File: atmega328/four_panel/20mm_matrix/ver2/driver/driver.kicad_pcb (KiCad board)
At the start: 2 copper layers, 40 x 40 mm, 52 parts, among them IC1 ATMEGA328P-M, IC2 ATMEGA328P-M, IC3 ATMEGA328P-M, IC4 ATMEGA328P-M, X1 CER_RESO, X2 CER_RESO, X3 CER_RESO, X4 CER_RESO

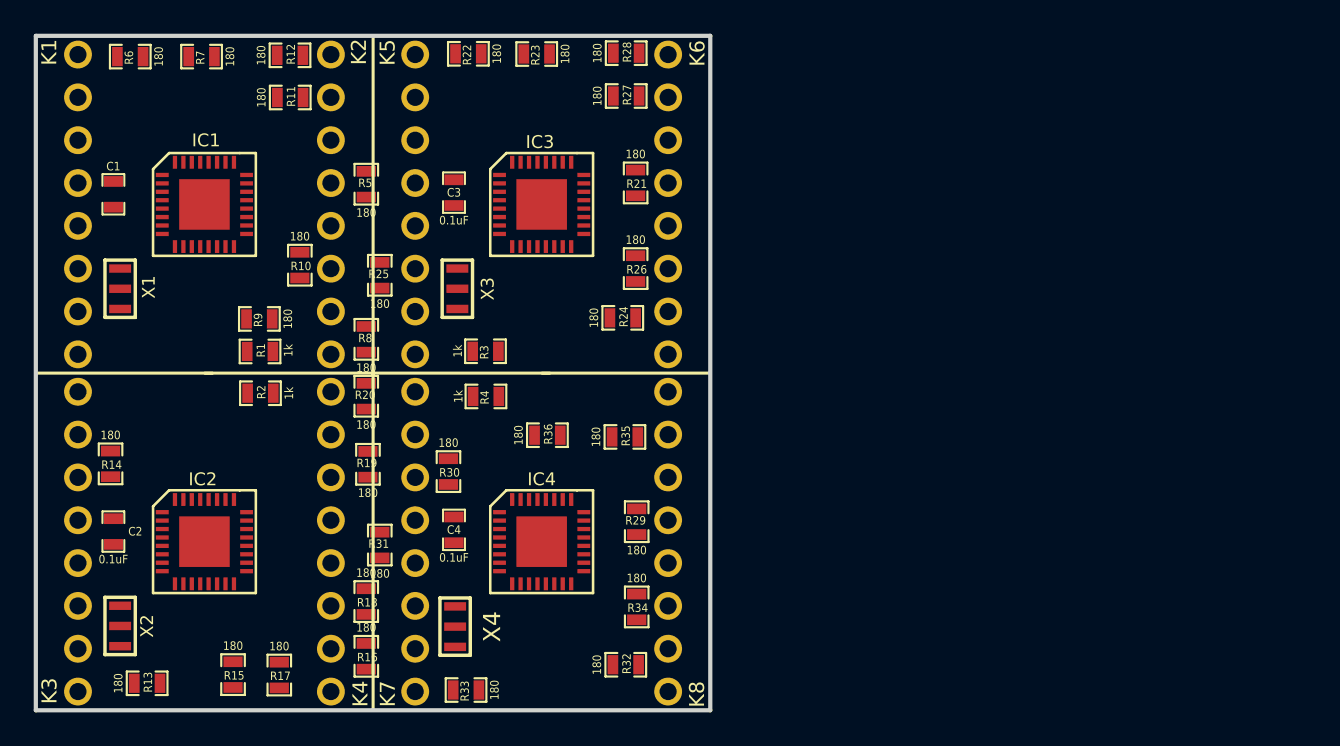
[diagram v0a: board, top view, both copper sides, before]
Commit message: Worked on ver2 of atmega328 4x20mm driver and comm pcbs.
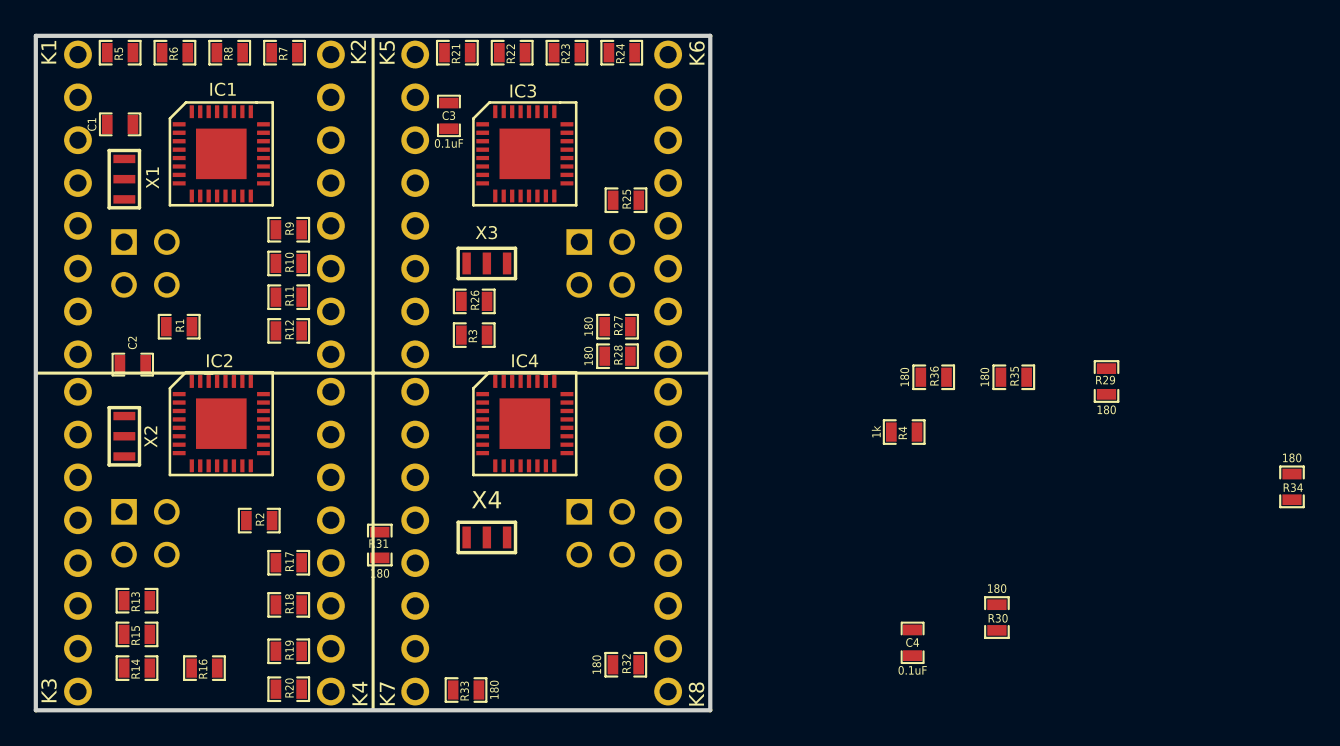
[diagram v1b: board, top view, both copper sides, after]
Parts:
- added P1: CONN_2X2, PIN_ARRAY_2X2, B.Cu at (56.5, 63.5)
- added P2: CONN_2X2, PIN_ARRAY_2X2, B.Cu at (56.5, 79.5)
- added P3: CONN_2X2, PIN_ARRAY_2X2, B.Cu at (83.5, 63.5)
- added P4: CONN_2X2, PIN_ARRAY_2X2, B.Cu at (83.5, 79.5)
- moved R34 39.5 mm to (124.5, 76.8)
- moved R30 33.7 mm to (107.0, 84.5)
- moved R29 29.1 mm to (113.5, 70.5)
- moved C4 28.0 mm to (102.0, 86.0)
- moved R4 24.9 mm to (101.5, 73.5)
- moved R35 23.3 mm to (108.0, 70.2)
- moved R36 23.2 mm to (103.2, 70.2)
- moved R8 18.8 mm to (61.5, 51.0), turned to 180 degrees
- moved R28 18.0 mm to (84.5, 69.0)
- moved R20 18.0 mm to (65.0, 88.8), turned to 0 degrees
- moved R5 16.6 mm to (55.0, 51.0), turned to 180 degrees
- moved R12 16.3 mm to (65.0, 67.5)
- moved R24 15.7 mm to (84.8, 51.0), turned to 180 degrees
- moved R25 15.3 mm to (85.0, 59.8), turned to 0 degrees
- moved R27 13.7 mm to (84.5, 67.2)
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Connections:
- net /XTAL1_DRV4 renamed /XTAL0_DRV3
- net /XTAL2_DRV1 renamed /XTAL1_DRV0
- IC1 pad 1: /COL4_DRV1 -> /ROW3_DRV0
- IC1 pad 10: /COL7_DRV1 -> /ROW6_DRV0
- IC1 pad 11: /COL8_DRV1 -> /ROW7_DRV0
- IC1 pad 12: /ROW1_DRV1 -> /COL6_DRV0
- IC1 pad 13: /ROW2_DRV1 -> /COL7_DRV0
- IC1 pad 14: /ROW3_DRV1 -> /CS0
- IC1 pad 15: /ROW4_DRV1 -> /MOSI
- IC1 pad 16: /ROW5_DRV1 -> /MISO
- IC1 pad 17: /ROW6_DRV1 -> /SCK
- IC1 pad 2: /COL5_DRV1 -> /ROW4_DRV0
- IC1 pad 23: /ROW7_DRV1 -> /COL0_DRV0
- IC1 pad 24: /ROW8_DRV1 -> /COL1_DRV0
- IC1 pad 25: /PCINT10/PC2 -> /COL2_DRV0
- IC1 pad 26: /PCINT11/PC3 -> /COL3_DRV0
- IC1 pad 27: /SDA -> /COL4_DRV0
- IC1 pad 28: /SCL -> /COL5_DRV0
- IC1 pad 29: /RESET_DRV1 -> /RESET_DRV0
- IC1 pad 30: /COL1_DRV1 -> /ROW0_DRV0
- IC1 pad 31: /COL2_DRV1 -> /ROW1_DRV0
- IC1 pad 32: /COL3_DRV1 -> /ROW2_DRV0
- IC1 pad 7: /XTAL1_DRV1 -> /XTAL0_DRV0
- IC1 pad 9: /COL6_DRV1 -> /ROW5_DRV0
- IC2 pad 1: /COL4_DRV2 -> /ROW3_DRV1
- IC2 pad 10: /COL7_DRV2 -> /ROW6_DRV1
- IC2 pad 11: /COL8_DRV2 -> /ROW7_DRV1
- IC2 pad 12: /ROW1_DRV2 -> /COL6_DRV1
- IC2 pad 13: /ROW2_DRV2 -> /COL7_DRV1
- IC2 pad 14: /ROW3_DRV2 -> /CS1
- IC2 pad 15: /ROW4_DRV2 -> /MOSI
- IC2 pad 16: /ROW5_DRV2 -> /MISO
- IC2 pad 17: /ROW6_DRV2 -> /SCK
- IC2 pad 2: /COL5_DRV2 -> /ROW4_DRV1
- IC2 pad 23: /ROW7_DRV2 -> /COL0_DRV1
- IC2 pad 24: /ROW8_DRV2 -> /COL1_DRV1
- IC2 pad 25: /PCINT10/PC2 -> /COL2_DRV1
- IC2 pad 26: /PCINT11/PC3 -> /COL3_DRV1
- IC2 pad 27: /SDA -> /COL4_DRV1
- IC2 pad 28: /SCL -> /COL5_DRV1
- IC2 pad 29: /RESET_DRV2 -> /RESET_DRV1
- IC2 pad 30: /COL1_DRV2 -> /ROW0_DRV1
- IC2 pad 31: /COL2_DRV2 -> /ROW1_DRV1
- IC2 pad 32: /COL3_DRV2 -> /ROW2_DRV1
- IC2 pad 7: /XTAL1_DRV2 -> /XTAL0_DRV1
- IC2 pad 8: /XTAL2_DRV2 -> /XTAL1_DRV1
- IC2 pad 9: /COL6_DRV2 -> /ROW5_DRV1
- IC3 pad 1: /COL4_DRV3 -> /ROW3_DRV2
- IC3 pad 10: /COL7_DRV3 -> /ROW6_DRV2
- IC3 pad 11: /COL8_DRV3 -> /ROW7_DRV2
- IC3 pad 12: /ROW1_DRV3 -> /COL6_DRV2
- IC3 pad 13: /ROW2_DRV3 -> /COL7_DRV2
- IC3 pad 14: /ROW3_DRV3 -> /CS2
- IC3 pad 15: /ROW4_DRV3 -> /MOSI
- IC3 pad 16: /ROW5_DRV3 -> /MISO
- IC3 pad 17: /ROW6_DRV3 -> /SCK
- IC3 pad 2: /COL5_DRV3 -> /ROW4_DRV2
- IC3 pad 23: /ROW7_DRV3 -> /COL0_DRV2
- IC3 pad 24: /ROW8_DRV3 -> /COL1_DRV2
- IC3 pad 25: /PCINT10/PC2 -> /COL2_DRV2
- IC3 pad 26: /PCINT11/PC3 -> /COL3_DRV2
- IC3 pad 27: /SDA -> /COL4_DRV2
- IC3 pad 28: /SCL -> /COL5_DRV2
- IC3 pad 29: /RESET_DRV3 -> /RESET_DRV0
- IC3 pad 30: /COL1_DRV3 -> /ROW0_DRV2
- IC3 pad 31: /COL2_DRV3 -> /ROW1_DRV2
- IC3 pad 32: /COL3_DRV3 -> /ROW2_DRV2
- IC3 pad 7: /XTAL1_DRV3 -> /XTAL0_DRV2
- IC3 pad 8: /XTAL2_DRV3 -> /XTAL1_DRV2
- IC3 pad 9: /COL6_DRV3 -> /ROW5_DRV2
- IC4 pad 1: /COL4_DRV4 -> /ROW4_DRV3
- IC4 pad 10: /COL7_DRV4 -> /ROW7_DRV3
- IC4 pad 11: /COL8_DRV4 -> /ROW8_DRV3
- IC4 pad 12: /ROW1_DRV4 -> /COL7_DRV3
- IC4 pad 13: /ROW2_DRV4 -> /COL8_DRV3
- IC4 pad 14: /ROW3_DRV4 -> /CS3
- IC4 pad 15: /ROW4_DRV4 -> /MOSI
- IC4 pad 16: /ROW5_DRV4 -> /MISO
- IC4 pad 17: /ROW6_DRV4 -> /SCK
- IC4 pad 2: /COL5_DRV4 -> /ROW5_DRV3
- IC4 pad 23: /ROW7_DRV4 -> /COL1_DRV3
- IC4 pad 24: /ROW8_DRV4 -> /COL2_DRV3
- IC4 pad 25: /PCINT10/PC2 -> /COL3_DRV3
- IC4 pad 26: /PCINT11/PC3 -> /COL4_DRV3
- IC4 pad 27: /SDA -> /COL5_DRV3
- IC4 pad 28: /SCL -> /COL6_DRV3
- IC4 pad 29: /RESET_DRV4 -> /RESET_DRV3
- IC4 pad 30: /COL1_DRV4 -> /ROW0_DRV3
- IC4 pad 31: /COL2_DRV4 -> /ROW2_DRV3
- IC4 pad 32: /COL3_DRV4 -> /ROW3_DRV3
- IC4 pad 8: /XTAL2_DRV4 -> /XTAL1_DRV3
- IC4 pad 9: /COL6_DRV4 -> /ROW6_DRV3
- MATRIX1 pad 1: /COL5_DRV1 -> N-0000095
- MATRIX1 pad 10: N-0000092 -> N-0000081
- MATRIX1 pad 12: /COL4_DRV1 -> N-0000079
- MATRIX1 pad 13: N-0000091 -> /COL7_DRV0
- MATRIX1 pad 14: /COL2_DRV1 -> /COL6_DRV0
- MATRIX1 pad 15: N-00000105 (its old number) -> /COL5_DRV0
- MATRIX1 pad 16: N-00000106 -> /COL4_DRV0
- MATRIX1 pad 2: /COL7_DRV1 -> N-0000096
- MATRIX1 pad 3: N-0000089 -> N-0000097
- MATRIX1 pad 4: N-0000090 -> N-0000078
- MATRIX1 pad 5: /COL8_DRV1 -> /COL0_DRV0
- MATRIX1 pad 6: N-00000103 -> /COL1_DRV0
- MATRIX1 pad 7: /COL6_DRV1 -> /COL2_DRV0
- MATRIX1 pad 8: /COL3_DRV1 -> /COL3_DRV0
- MATRIX1 pad 9: /COL1_DRV1 -> N-0000082
- MATRIX2 pad 1: /COL5_DRV2 -> N-00000110
- MATRIX2 pad 10: N-0000098 -> N-00000106
- MATRIX2 pad 12: /COL4_DRV2 -> N-00000113
- MATRIX2 pad 13: N-0000095 -> /COL7_DRV1
- MATRIX2 pad 14: /COL2_DRV2 -> /COL6_DRV1
- MATRIX2 pad 15: N-00000101 -> /COL5_DRV1
- MATRIX2 pad 16: N-00000102 -> /COL4_DRV1
- MATRIX2 pad 2: /COL7_DRV2 -> N-00000108
- MATRIX2 pad 3: N-0000096 -> N-00000109
- MATRIX2 pad 4: N-0000097 -> N-00000111
- MATRIX2 pad 5: /COL8_DRV2 -> /COL0_DRV1
- MATRIX2 pad 6: N-0000099 -> /COL1_DRV1
- MATRIX2 pad 7: /COL6_DRV2 -> /COL2_DRV1
- MATRIX2 pad 8: /COL3_DRV2 -> /COL3_DRV1
- MATRIX2 pad 9: /COL1_DRV2 -> N-00000107
- MATRIX3 pad 1: /COL5_DRV3 -> N-00000112
- MATRIX3 pad 10: N-0000081 -> N-00000119
- MATRIX3 pad 12: /COL4_DRV3 -> N-00000117
- MATRIX3 pad 13: N-0000080 (its old number) -> /COL7_DRV2
- MATRIX3 pad 14: /COL2_DRV3 -> /COL6_DRV2
- MATRIX3 pad 15: N-0000045 -> /COL5_DRV2
- MATRIX3 pad 16: N-0000046 (its old number) -> /COL4_DRV2
- MATRIX3 pad 2: /COL7_DRV3 -> N-00000115
- MATRIX3 pad 3: N-0000078 -> N-00000116
- MATRIX3 pad 4: N-0000079 -> N-00000114
- MATRIX3 pad 5: /COL8_DRV3 -> /COL0_DRV2
- MATRIX3 pad 6: N-0000073 (its old number) -> /COL1_DRV2
- MATRIX3 pad 7: /COL6_DRV3 -> /COL2_DRV2
- MATRIX3 pad 8: /COL3_DRV3 -> /COL3_DRV2
- MATRIX3 pad 9: /COL1_DRV3 -> N-00000120
- MATRIX4 pad 1: /COL5_DRV4 -> N-0000088
- MATRIX4 pad 10: N-0000077 -> N-0000045
- MATRIX4 pad 12: /COL4_DRV4 -> N-0000047
- MATRIX4 pad 13: N-0000076 -> /COL7_DRV3
- MATRIX4 pad 14: /COL2_DRV4 -> /COL6_DRV3
- MATRIX4 pad 15: N-0000071 -> /COL5_DRV3
- MATRIX4 pad 16: N-0000072 -> /COL4_DRV3
- MATRIX4 pad 2: /COL7_DRV4 -> N-0000084
- MATRIX4 pad 3: N-0000074 -> N-0000086
- MATRIX4 pad 4: N-0000075 -> N-0000090
- MATRIX4 pad 5: /COL8_DRV4 -> /COL0_DRV3
- MATRIX4 pad 6: N-0000065 -> /COL1_DRV3
- MATRIX4 pad 7: /COL6_DRV4 -> /COL2_DRV3
- MATRIX4 pad 8: /COL3_DRV4 -> /COL3_DRV3
- MATRIX4 pad 9: /COL1_DRV4 -> N-0000044
- R1 pad 1: /RESET_DRV1 -> /RESET_DRV0
- R10 pad 1: /ROW6_DRV1 -> /ROW5_DRV0
- R11 pad 1: /ROW7_DRV1 -> /ROW6_DRV0
- R11 pad 2: N-00000105 (its old number) -> N-0000081
- R12 pad 1: /ROW8_DRV1 -> /ROW7_DRV0
- R12 pad 2: N-00000106 -> N-0000082
- R13 pad 1: /ROW1_DRV2 -> /ROW0_DRV1
- R13 pad 2: N-0000095 -> N-00000110
- R14 pad 1: /ROW2_DRV2 -> /ROW1_DRV1
- R14 pad 2: N-0000096 -> N-00000108
- R15 pad 1: /ROW3_DRV2 -> /ROW2_DRV1
- R15 pad 2: N-0000097 -> N-00000109
- R16 pad 1: /ROW4_DRV2 -> /ROW3_DRV1
- R16 pad 2: N-0000098 -> N-00000111
- R17 pad 1: /ROW5_DRV2 -> /ROW4_DRV1
- R17 pad 2: N-0000099 -> N-00000113
- R18 pad 1: /ROW6_DRV2 -> /ROW5_DRV1
- R19 pad 1: /ROW7_DRV2 -> /ROW6_DRV1
- R19 pad 2: N-00000101 -> N-00000106
- R2 pad 1: /RESET_DRV2 -> /RESET_DRV1
- R20 pad 1: /ROW8_DRV2 -> /ROW7_DRV1
- R20 pad 2: N-00000102 -> N-00000107
- R21 pad 1: /ROW1_DRV3 -> /ROW0_DRV2
- R21 pad 2: N-0000080 (its old number) -> N-00000112
- R22 pad 1: /ROW2_DRV3 -> /ROW1_DRV2
- R22 pad 2: N-0000078 -> N-00000115
- R23 pad 1: /ROW3_DRV3 -> /ROW2_DRV2
- R23 pad 2: N-0000079 -> N-00000116
- R24 pad 1: /ROW4_DRV3 -> /ROW3_DRV2
- R24 pad 2: N-0000081 -> N-00000114
- R25 pad 1: /ROW5_DRV3 -> /ROW4_DRV2
- R25 pad 2: N-0000073 (its old number) -> N-00000117
- R26 pad 1: /ROW6_DRV3 -> /ROW5_DRV2
- R27 pad 1: /ROW7_DRV3 -> /ROW6_DRV2
- R27 pad 2: N-0000045 -> N-00000119
- R28 pad 1: /ROW8_DRV3 -> /ROW7_DRV2
- R28 pad 2: N-0000046 (its old number) -> N-00000120
- R29 pad 1: /ROW1_DRV4 -> /ROW0_DRV3
- R29 pad 2: N-0000076 -> N-0000088
- R3 pad 1: /RESET_DRV3 -> /RESET_DRV0
- R30 pad 1: /ROW2_DRV4 -> /ROW1_DRV3
- R30 pad 2: N-0000074 -> N-0000084
- R31 pad 1: /ROW3_DRV4 -> /ROW2_DRV3
- R31 pad 2: N-0000075 -> N-0000086
- R32 pad 1: /ROW4_DRV4 -> /ROW3_DRV3
- R32 pad 2: N-0000077 -> N-0000090
- R33 pad 1: /ROW5_DRV4 -> /ROW4_DRV3
- R33 pad 2: N-0000065 -> N-0000047
- R34 pad 1: /ROW6_DRV4 -> /ROW5_DRV3
- R35 pad 1: /ROW7_DRV4 -> /ROW6_DRV3
- R35 pad 2: N-0000071 -> N-0000045
- R36 pad 1: /ROW8_DRV4 -> /ROW7_DRV3
- R36 pad 2: N-0000072 -> N-0000044
- R4 pad 1: /RESET_DRV4 -> /RESET_DRV3
- R5 pad 1: /ROW1_DRV1 -> /ROW0_DRV0
- R5 pad 2: N-0000091 -> N-0000095
- R6 pad 1: /ROW2_DRV1 -> /ROW1_DRV0
- R6 pad 2: N-0000089 -> N-0000096
- R7 pad 1: /ROW3_DRV1 -> /ROW2_DRV0
- R7 pad 2: N-0000090 -> N-0000097
- R8 pad 1: /ROW4_DRV1 -> /ROW3_DRV0
- R8 pad 2: N-0000092 -> N-0000078
- R9 pad 1: /ROW5_DRV1 -> /ROW4_DRV0
- R9 pad 2: N-00000103 -> N-0000079
- X1 pad 1: /XTAL1_DRV1 -> /XTAL0_DRV0
- X2 pad 1: /XTAL1_DRV2 -> /XTAL0_DRV1
- X2 pad 3: /XTAL2_DRV2 -> /XTAL1_DRV1
- X3 pad 1: /XTAL1_DRV3 -> /XTAL0_DRV2
- X3 pad 3: /XTAL2_DRV3 -> /XTAL1_DRV2
- X4 pad 3: /XTAL2_DRV4 -> /XTAL1_DRV3

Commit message: Finished preliminary version 2.0 of atmega328 4x20mm panels design.
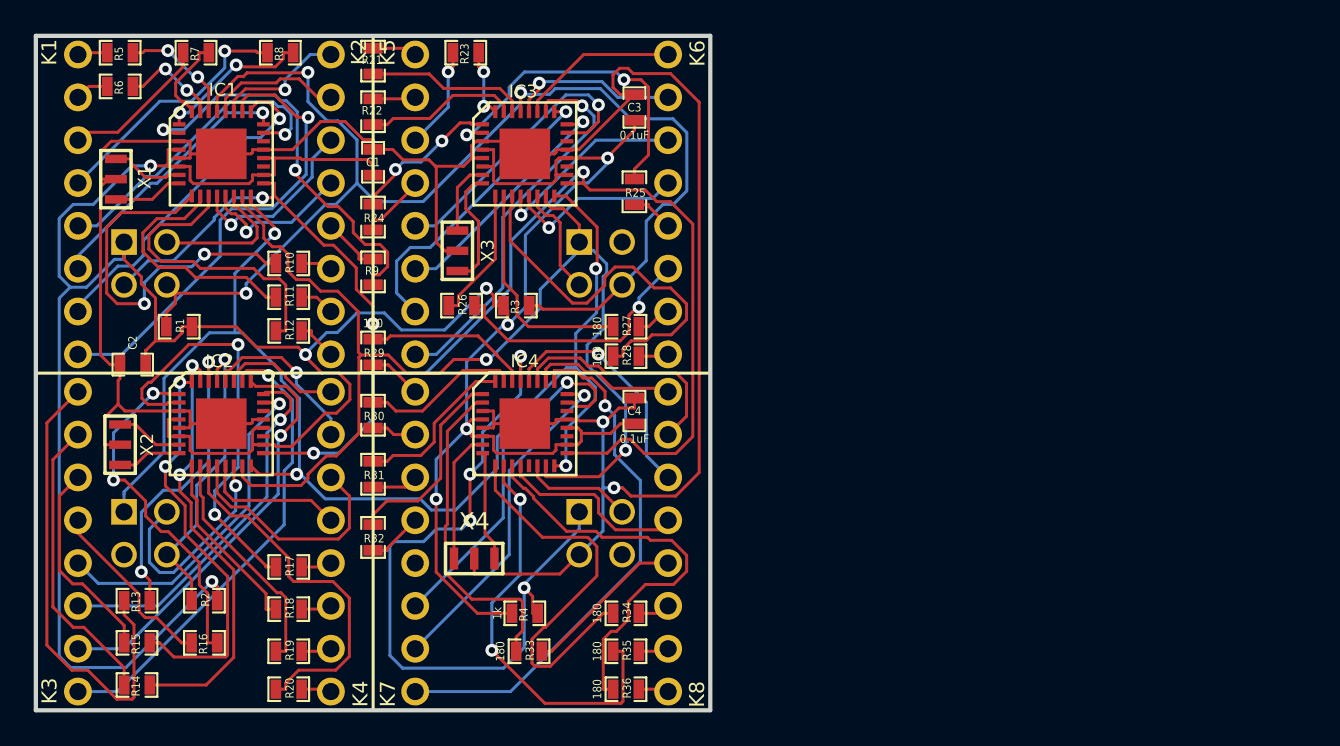
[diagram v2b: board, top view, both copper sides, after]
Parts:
- moved R29 43.5 mm to (70.0, 68.8), turned to 270 degrees
- moved R34 40.2 mm to (85.0, 84.2), turned to 0 degrees
- moved R30 38.9 mm to (70.0, 72.5)
- moved R35 28.2 mm to (85.0, 86.5)
- moved R36 26.0 mm to (85.0, 88.8)
- moved R4 24.9 mm to (79.0, 84.2)
- moved C4 21.5 mm to (85.5, 72.2)
- moved R24 17.7 mm to (70.0, 60.8), turned to 270 degrees
- moved R32 16.8 mm to (70.0, 79.8), turned to 270 degrees
- moved C1 15.2 mm to (70.0, 57.5), turned to 90 degrees
- moved C3 11.0 mm to (85.5, 54.2)
- moved R22 8.96 mm to (70.0, 54.5), turned to 90 degrees
- moved R23 6.00 mm to (75.5, 51.0)
- moved R2 5.76 mm to (60.0, 83.5)
- moved R9 5.59 mm to (70.0, 64.0), turned to 90 degrees
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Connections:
- IC4 pad 1: /ROW4_DRV3 -> /ROW3_DRV3
- IC4 pad 10: /ROW7_DRV3 -> /ROW6_DRV3
- IC4 pad 11: /ROW8_DRV3 -> /ROW7_DRV3
- IC4 pad 2: /ROW5_DRV3 -> /ROW4_DRV3
- IC4 pad 31: /ROW2_DRV3 -> /ROW1_DRV3
- IC4 pad 32: /ROW3_DRV3 -> /ROW2_DRV3
- IC4 pad 9: /ROW6_DRV3 -> /ROW5_DRV3
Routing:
- net +5V: track 0.00 -> 189.2 mm, vias 0 -> 8
- net GND: track 0.00 -> 141.2 mm, vias 0 -> 2
- net /SCK: track 0.00 -> 85.3 mm, vias 0 -> 4
- net /MISO: track 0.00 -> 79.0 mm, vias 0 -> 4
- net /RESET_DRV0: track 0.00 -> 74.4 mm, vias 0 -> 3
- net /MOSI: track 0.00 -> 69.6 mm, vias 0 -> 2
- net /RESET_DRV3: track 0.00 -> 44.6 mm, vias 0 -> 4
- net /COL3_DRV3: track 0.00 -> 31.7 mm, vias 0 -> 1
- net N-00000109: track 0.00 -> 28.3 mm
- net /COL3_DRV1: track 0.00 -> 28.1 mm, vias 0 -> 1
- net /COL3_DRV0: track 0.00 -> 27.9 mm, vias 0 -> 1
- net /ROW1_DRV1: track 0.00 -> 25.8 mm, vias 0 -> 2
- net /ROW4_DRV1: track 0.00 -> 25.4 mm, vias 0 -> 2
- net /COL2_DRV1: track 0.00 -> 25.0 mm, vias 0 -> 1
- net /ROW7_DRV3: track 0.00 -> 24.7 mm
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
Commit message: Added ground pin header to backside of ver 2 com pcb.
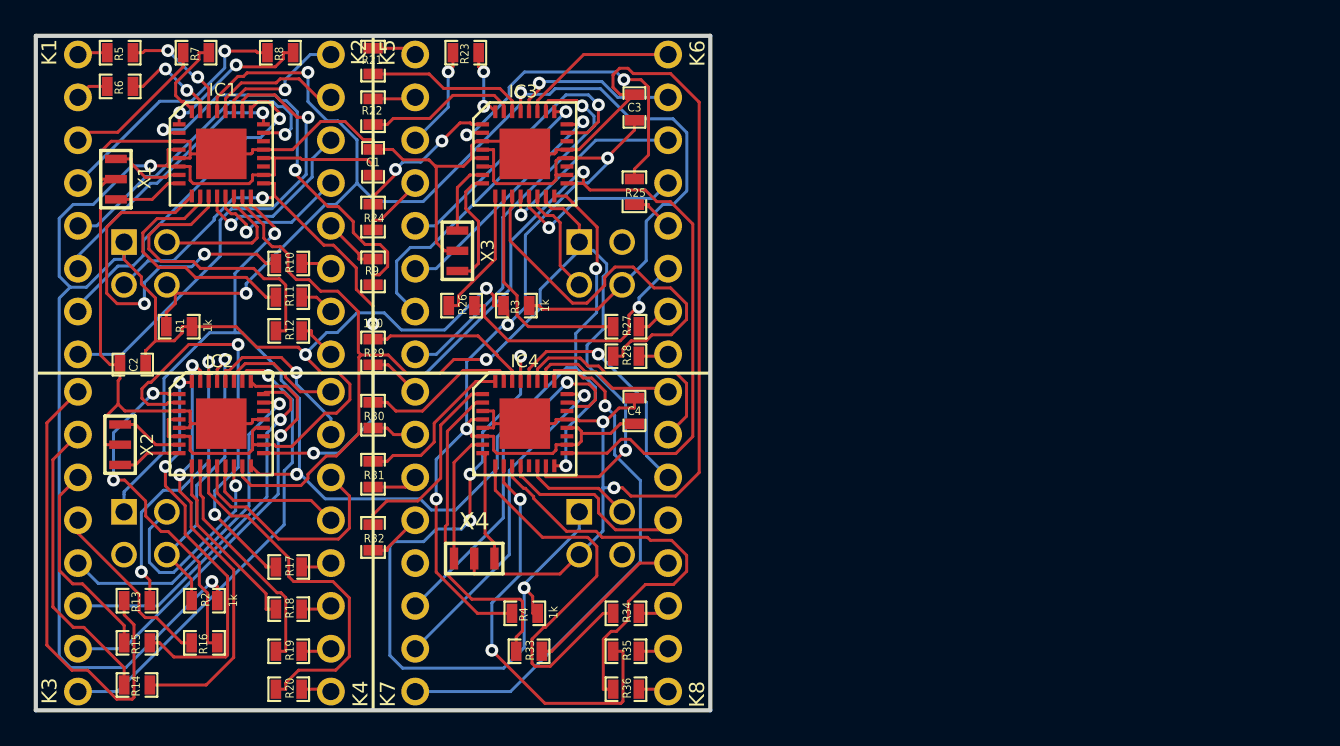
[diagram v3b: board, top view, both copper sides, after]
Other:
- board text added: "4-Matrix Atmega328 Driver V0.2 www.iorodeo.com"
- board text removed: "4-Matrix Atmega328 Driver V1.0 www.iorodeo.com"
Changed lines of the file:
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@@
     (at 55.75 69.5 180)
     (attr smd)
-    (fp_text reference C2 (at 0 1.3 270) (layer F.SilkS)
+    (fp_text reference C2 (at -0.05 0 270) (layer F.SilkS)
       (effects (font (size 0.508 0.4572) (thickness 0.1143)))
     )
@@
       (effects (font (size 0.508 0.4572) (thickness 0.1143)))
     )
-    (fp_text value 0.1uF (at -1.651 0 180) (layer F.SilkS)
+    (fp_text value 0.1uF (at -1.651 0 180) (layer F.SilkS) hide
       (effects (font (size 0.508 0.4572) (thickness 0.1143)))
     )
@@
       (effects (font (size 0.508 0.4572) (thickness 0.1143)))
     )
-    (fp_text value 0.1uF (at -1.651 0 180) (layer F.SilkS)
+    (fp_text value 0.1uF (at -1.651 0 180) (layer F.SilkS) hide
       (effects (font (size 0.508 0.4572) (thickness 0.1143)))
     )
@@
       (effects (font (size 0.50038 0.4572) (thickness 0.1143)))
     )
-    (fp_text value 180 (at -1.69926 0 90) (layer F.SilkS)
+    (fp_text value 180 (at -1.69926 0 90) (layer F.SilkS) hide
       (effects (font (size 0.508 0.4572) (thickness 0.1143)))
     )
@@
       (effects (font (size 0.50038 0.4572) (thickness 0.1143)))
     )
-    (fp_text value 180 (at -1.69926 0 90) (layer F.SilkS)
+    (fp_text value 180 (at -1.69926 0 90) (layer F.SilkS) hide
       (effects (font (size 0.508 0.4572) (thickness 0.1143)))
     )
@@
       (effects (font (size 0.50038 0.4572) (thickness 0.1143)))
     )
-    (fp_text value 180 (at -1.69926 0 90) (layer F.SilkS)
+    (fp_text value 180 (at -1.69926 0 90) (layer F.SilkS) hide
       (effects (font (size 0.508 0.4572) (thickness 0.1143)))
     )
@@
       (effects (font (size 0.50038 0.4572) (thickness 0.1143)))
     )
-    (fp_text value 180 (at -1.69926 0 90) (layer F.SilkS)
+    (fp_text value 180 (at -1.69926 0 90) (layer F.SilkS) hide
       (effects (font (size 0.508 0.4572) (thickness 0.1143)))
     )
@@
       (effects (font (size 0.50038 0.4572) (thickness 0.1143)))
     )
-    (fp_text value 180 (at -1.69926 0 90) (layer F.SilkS)
+    (fp_text value 180 (at -1.69926 0 90) (layer F.SilkS) hide
       (effects (font (size 0.508 0.4572) (thickness 0.1143)))
     )
@@
       (effects (font (size 0.50038 0.4572) (thickness 0.1143)))
     )
-    (fp_text value 180 (at -1.69926 0 90) (layer F.SilkS)
+    (fp_text value 180 (at -1.69926 0 90) (layer F.SilkS) hide
       (effects (font (size 0.508 0.4572) (thickness 0.1143)))
     )
@@
       (effects (font (size 0.50038 0.4572) (thickness 0.1143)))
     )
-    (fp_text value 1k (at 1.6256 0 270) (layer F.SilkS)
+    (fp_text value 1k (at -1.7 0.05 270) (layer F.SilkS)
       (effects (font (size 0.508 0.4572) (thickness 0.1143)))
     )
@@
       (effects (font (size 0.50038 0.4572) (thickness 0.1143)))
     )
-    (fp_text value 1k (at 1.6383 0.0127 270) (layer F.SilkS) hide
+    (fp_text value 1k (at -1.7 0 270) (layer F.SilkS)
       (effects (font (size 0.508 0.4572) (thickness 0.1143)))
     )
@@
       (effects (font (size 0.50038 0.4572) (thickness 0.1143)))
     )
-    (fp_text value 1k (at 1.7018 0 90) (layer F.SilkS) hide
+    (fp_text value 1k (at 1.7018 0 90) (layer F.SilkS)
       (effects (font (size 0.508 0.4572) (thickness 0.1143)))
     )
@@
       (effects (font (size 0.50038 0.4572) (thickness 0.1143)))
     )
-    (fp_text value 1k (at 1.6891 -0.0635 90) (layer F.SilkS) hide
+    (fp_text value 1k (at 1.7 -0.05 90) (layer F.SilkS)
       (effects (font (size 0.508 0.4572) (thickness 0.1143)))
     )
@@
     (effects (font (size 0.889 0.889) (thickness 0.2032)))
   )
-  (gr_text "4-Matrix Atmega328 Driver V1.0\nwww.iorodeo.com" (at 63.5 70 90) (layer B.SilkS)
+  (gr_text "4-Matrix Atmega328 Driver V0.2\nwww.iorodeo.com" (at 63.5 70 90) (layer B.SilkS)
     (effects (font (size 1.016 1.016) (thickness 0.2032)) (justify mirror))
   )
@@
   (segment (start 60.7511 69.7852) (end 61.2145 69.3218) (width 0.1778) (layer F.Cu) (net 42))
   (segment (start 60.7511 70.5006) (end 60.7511 69.7852) (width 0.1778) (layer F.Cu) (net 42))
-  (segment (start 78.75108 70.50064) (end 78.75108 69.00108) (width 0.1778) (layer F.Cu) (net 43) (status 400000))
+  (segment (start 78.75108 70.50064) (end 78.75108 69.00108) (width 0.1778) (layer F.Cu) (net 43))
   (segment (start 78.9631 86.2869) (end 78.9631 82.741) (width 0.1778) (layer B.Cu) (net 43))
   (segment (start 77.75 87.5) (end 78.9631 86.2869) (width 0.1778) (layer B.Cu) (net 43))
@@
   (segment (start 57.1158 74.2497) (end 55.9172 73.0511) (width 0.1778) (layer F.Cu) (net 78))
   (segment (start 57.8526 74.2497) (end 57.1158 74.2497) (width 0.1778) (layer F.Cu) (net 78))
-  (segment (start 75 61.55112) (end 75 59) (width 0.1778) (layer F.Cu) (net 79) (status 400000))
-  (segment (start 75.75032 58.24968) (end 76.50064 58.24968) (width 0.1778) (layer F.Cu) (net 79) (status 800000))
+  (segment (start 75 61.55112) (end 75 59) (width 0.1778) (layer F.Cu) (net 79))
+  (segment (start 75.75032 58.24968) (end 76.50064 58.24968) (width 0.1778) (layer F.Cu) (net 79))
   (segment (start 75 59) (end 75.75032 58.24968) (width 0.1778) (layer F.Cu) (net 79))
   (segment (start 76.5006 74.2497) (end 75.8526 74.2497) (width 0.1778) (layer F.Cu) (net 80))
@@
   (segment (start 56.616 74.7501) (end 55.9172 75.4489) (width 0.1778) (layer F.Cu) (net 82))
   (segment (start 57.8526 74.7501) (end 56.616 74.7501) (width 0.1778) (layer F.Cu) (net 82))
-  (segment (start 75 63.94888) (end 75.80112 63.94888) (width 0.1778) (layer F.Cu) (net 83) (status 400000))
-  (segment (start 75.99994 58.75006) (end 76.50064 58.75006) (width 0.1778) (layer F.Cu) (net 83) (status 800000))
+  (segment (start 75 63.94888) (end 75.80112 63.94888) (width 0.1778) (layer F.Cu) (net 83))
+  (segment (start 75.99994 58.75006) (end 76.50064 58.75006) (width 0.1778) (layer F.Cu) (net 83))
   (segment (start 75.5 59.25) (end 75.99994 58.75006) (width 0.1778) (layer F.Cu) (net 83))
   (segment (start 75.5 60.25) (end 75.5 59.25) (width 0.1778) (layer F.Cu) (net 83))
@@
   (segment (start 76.6422 79.5261) (end 76.6422 74.8917) (width 0.1778) (layer F.Cu) (net 84))
   (segment (start 77.1989 80.0828) (end 76.6422 79.5261) (width 0.1778) (layer F.Cu) (net 84))
-  (segment (start 75 62.75) (end 74.25 62.75) (width 0.1778) (layer F.Cu) (net 85) (status 400000))
+  (segment (start 75 62.75) (end 74.25 62.75) (width 0.1778) (layer F.Cu) (net 85))
   (segment (start 73.75 62.25) (end 73.75 57.7354) (width 0.1778) (layer F.Cu) (net 85))
   (segment (start 74.25 62.75) (end 73.75 62.25) (width 0.1778) (layer F.Cu) (net 85))
